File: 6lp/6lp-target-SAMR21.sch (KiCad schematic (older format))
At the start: 25 parts, among them SW1 SW_PUSH, T1 2450BM15A0015, U3 SAMR21E, X1 CRYSTAL-4

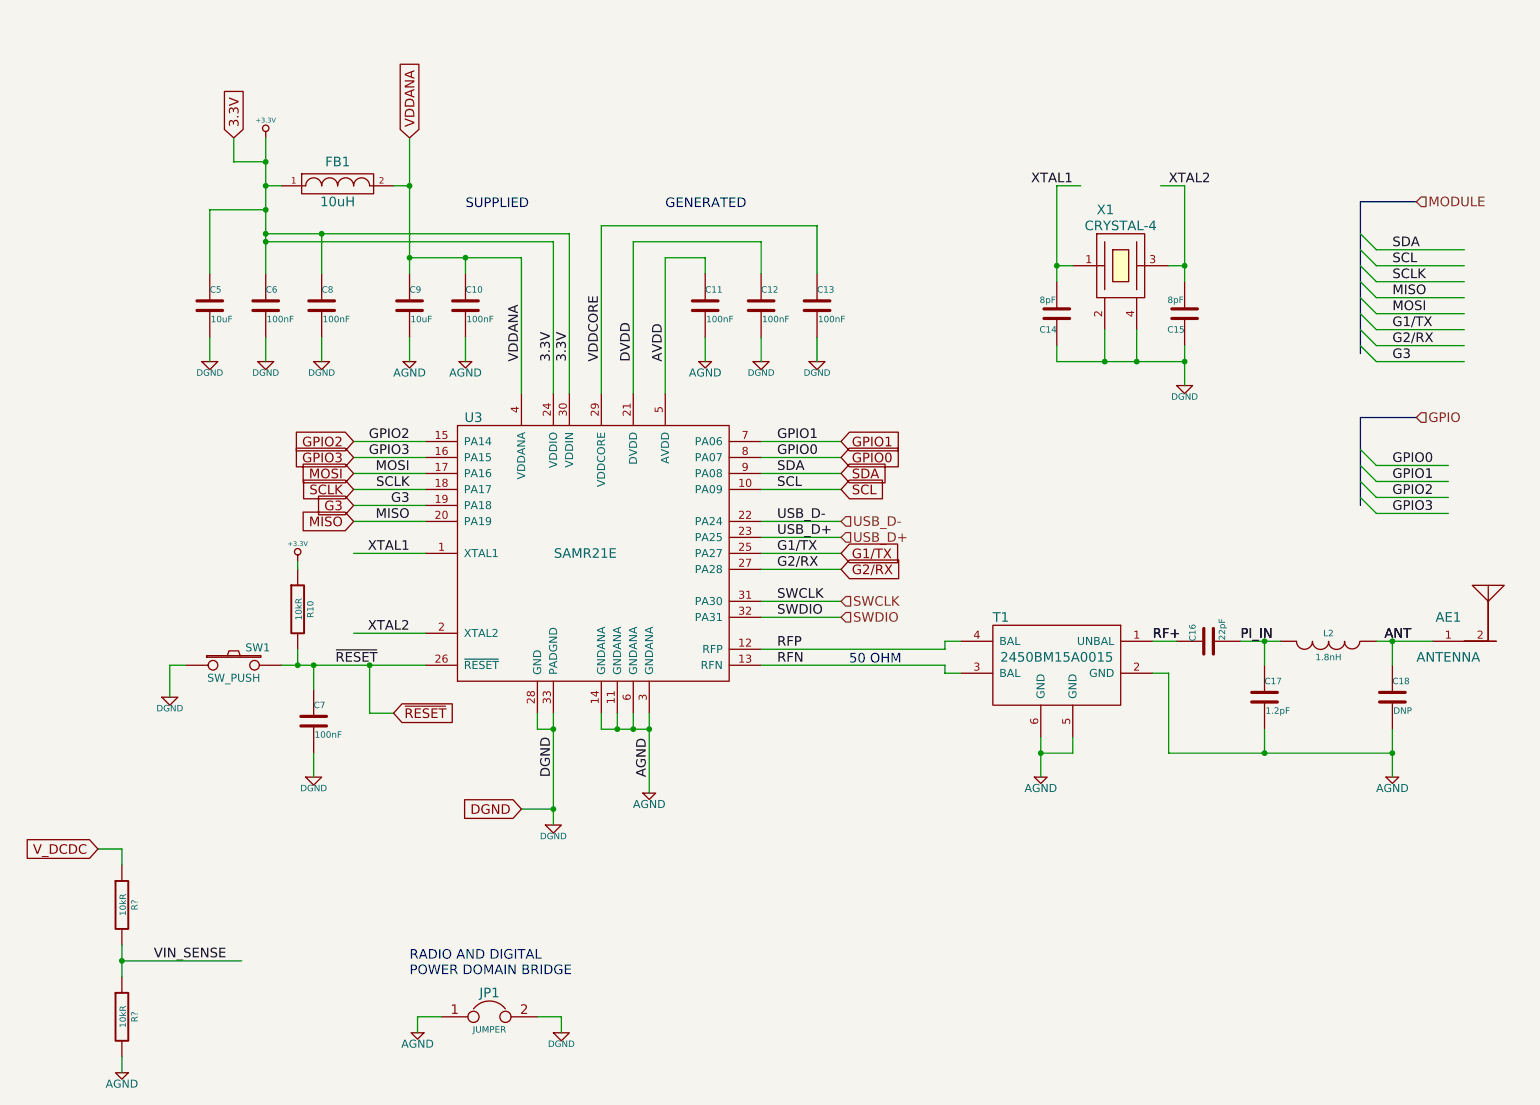
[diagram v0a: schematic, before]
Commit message: gpio rehash, netlist and component update
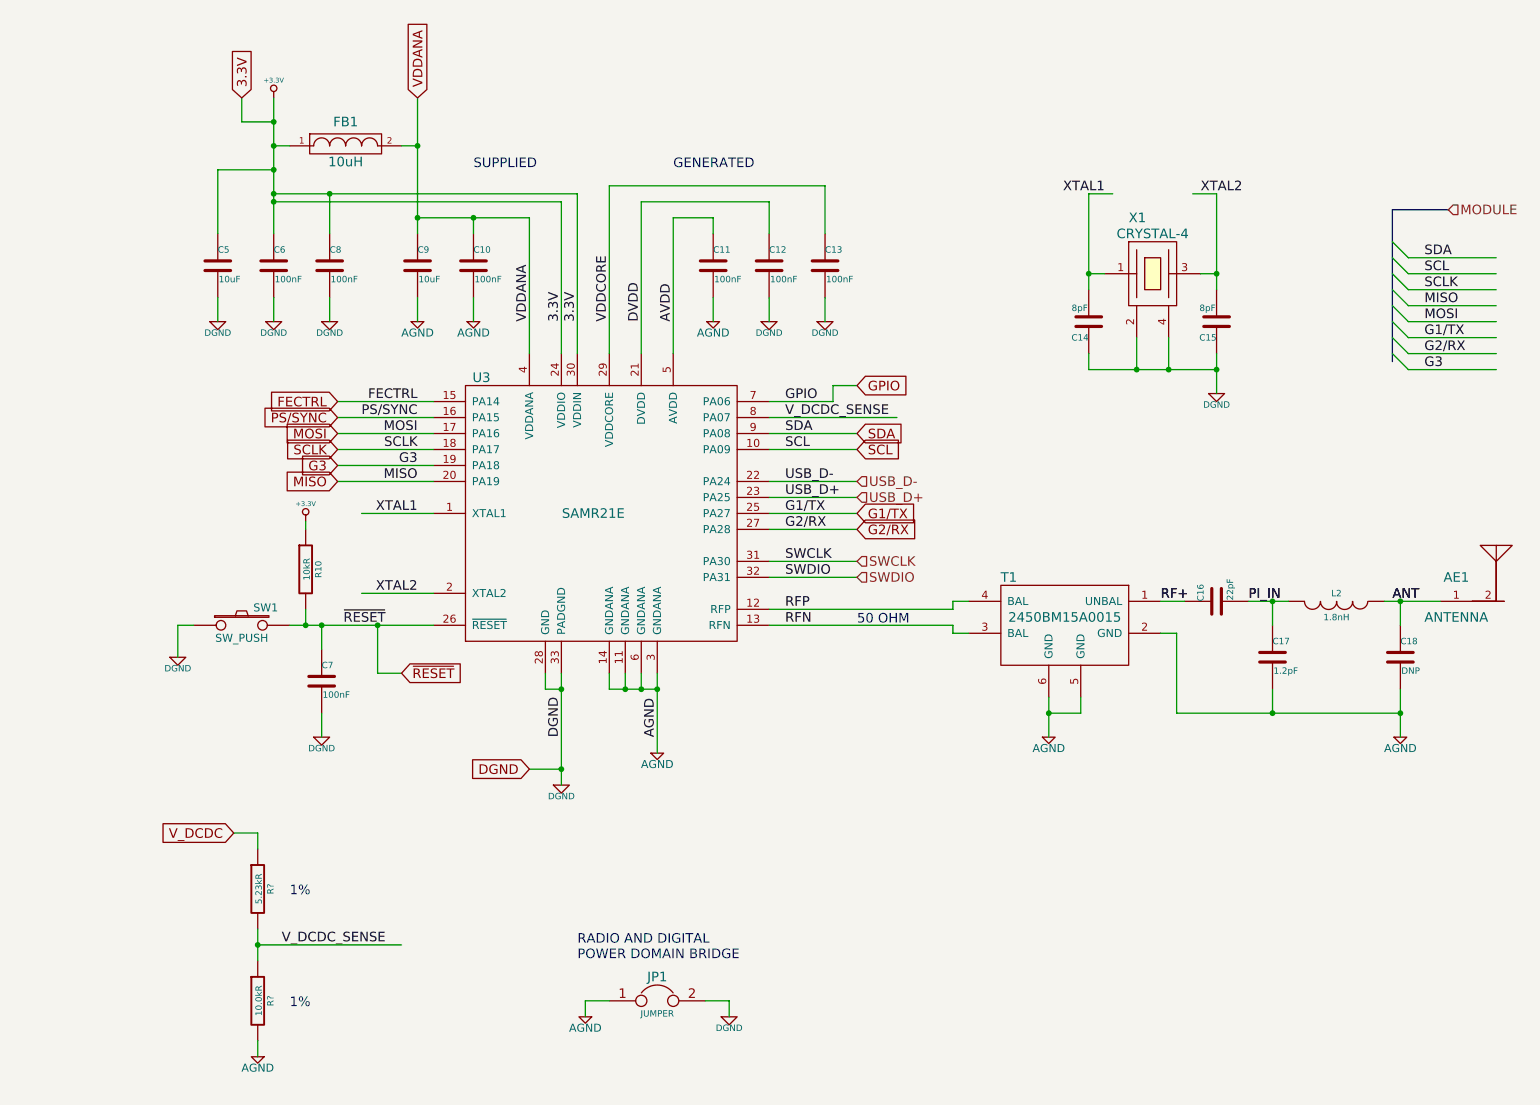
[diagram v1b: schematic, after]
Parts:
- R?: value 10kR -> 5.23kR
- R?: value 10kR -> 10.0kR
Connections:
- net labels added: FECTRL, PS/SYNC, V_DCDC_SENSE
- net labels removed: GPIO0, GPIO1, GPIO2, GPIO3, VIN_SENSE
- wire segments 120 -> 118
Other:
- note added: "1%"
- moved on the sheet: AE1, C10, C11, C12, C13, C14, C15, C16, C17, C18, C5, C6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

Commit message: don't sass me, DRC
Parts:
- gave numbers to parts that had none: 2
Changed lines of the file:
@@
 $EndDescr
 $Comp
-L AGND #PWR025
+L AGND #PWR024
 U 1 1 5453137E
 P 4700 5500
-F 0 "#PWR025" H 4700 5500 40  0001 C CNN
+F 0 "#PWR024" H 4700 5500 40  0001 C CNN
 F 1 "AGND" H 4700 5430 50  0000 C CNN
 F 2 "" H 4700 5500 60  0000 C CNN
@@
 $EndComp
 $Comp
-L DGND #PWR026
+L DGND #PWR025
 U 1 1 5453138D
 P 4100 5700
-F 0 "#PWR026" H 4100 5700 40  0001 C CNN
+F 0 "#PWR025" H 4100 5700 40  0001 C CNN
 F 1 "DGND" H 4100 5630 40  0000 C CNN
 F 2 "" H 4100 5700 60  0000 C CNN
@@
 $EndComp
 $Comp
-L DGND #PWR027
+L DGND #PWR026
 U 1 1 54531393
 P 2650 2800
-F 0 "#PWR027" H 2650 2800 40  0001 C CNN
+F 0 "#PWR026" H 2650 2800 40  0001 C CNN
 F 1 "DGND" H 2650 2730 40  0000 C CNN
 F 2 "" H 2650 2800 60  0000 C CNN
@@
 $EndComp
 $Comp
-L AGND #PWR028
+L AGND #PWR027
 U 1 1 545313BC
 P 5050 2800
-F 0 "#PWR028" H 5050 2800 40  0001 C CNN
+F 0 "#PWR027" H 5050 2800 40  0001 C CNN
 F 1 "AGND" H 5050 2730 50  0000 C CNN
 F 2 "" H 5050 2800 60  0000 C CNN
@@
 $EndComp
 $Comp
-L DGND #PWR029
+L DGND #PWR028
 U 1 1 545313C2
 P 2300 2800
-F 0 "#PWR029" H 2300 2800 40  0001 C CNN
+F 0 "#PWR028" H 2300 2800 40  0001 C CNN
 F 1 "DGND" H 2300 2730 40  0000 C CNN
 F 2 "" H 2300 2800 60  0000 C CNN
@@
 $EndComp
 $Comp
-L DGND #PWR030
+L DGND #PWR029
 U 1 1 545313C8
 P 5750 2800
-F 0 "#PWR030" H 5750 2800 40  0001 C CNN
+F 0 "#PWR029" H 5750 2800 40  0001 C CNN
 F 1 "DGND" H 5750 2730 40  0000 C CNN
 F 2 "" H 5750 2800 60  0000 C CNN
@@
 $EndComp
 $Comp
-L +3.3V #PWR031
+L +3.3V #PWR030
 U 1 1 545313CE
 P 2300 1400
-F 0 "#PWR031" H 2300 1360 30  0001 C CNN
+F 0 "#PWR030" H 2300 1360 30  0001 C CNN
 F 1 "+3.3V" H 2300 1510 30  0000 C CNN
 F 2 "" H 2300 1400 60  0000 C CNN
@@
 AVDD
 $Comp
-L DGND #PWR032
+L DGND #PWR031
 U 1 1 545313D5
 P 5400 2800
-F 0 "#PWR032" H 5400 2800 40  0001 C CNN
+F 0 "#PWR031" H 5400 2800 40  0001 C CNN
 F 1 "DGND" H 5400 2730 40  0000 C CNN
 F 2 "" H 5400 2800 60  0000 C CNN
@@
 SUPPLIED
 $Comp
-L AGND #PWR033
+L AGND #PWR032
 U 1 1 545313DF
 P 3550 2800
-F 0 "#PWR033" H 3550 2800 40  0001 C CNN
+F 0 "#PWR032" H 3550 2800 40  0001 C CNN
 F 1 "AGND" H 3550 2730 50  0000 C CNN
 F 2 "" H 3550 2800 60  0000 C CNN
@@
 $EndComp
 $Comp
-L AGND #PWR034
+L AGND #PWR033
 U 1 1 545313F5
 P 3200 2800
-F 0 "#PWR034" H 3200 2800 40  0001 C CNN
+F 0 "#PWR033" H 3200 2800 40  0001 C CNN
 F 1 "AGND" H 3200 2730 50  0000 C CNN
 F 2 "" H 3200 2800 60  0000 C CNN
@@
 $EndComp
 $Comp
-L DGND #PWR035
+L DGND #PWR034
 U 1 1 54531403
 P 1950 2800
-F 0 "#PWR035" H 1950 2800 40  0001 C CNN
+F 0 "#PWR034" H 1950 2800 40  0001 C CNN
 F 1 "DGND" H 1950 2730 40  0000 C CNN
 F 2 "" H 1950 2800 60  0000 C CNN
@@
 $EndComp
 $Comp
-L DGND #PWR036
+L DGND #PWR035
 U 1 1 54531418
 P 2600 5400
-F 0 "#PWR036" H 2600 5400 40  0001 C CNN
+F 0 "#PWR035" H 2600 5400 40  0001 C CNN
 F 1 "DGND" H 2600 5330 40  0000 C CNN
 F 2 "" H 2600 5400 60  0000 C CNN
@@
 $EndComp
 $Comp
-L +3.3V #PWR037
+L +3.3V #PWR036
 U 1 1 54531425
 P 2500 4050
-F 0 "#PWR037" H 2500 4010 30  0001 C CNN
+F 0 "#PWR036" H 2500 4010 30  0001 C CNN
 F 1 "+3.3V" H 2500 4160 30  0000 C CNN
 F 2 "" H 2500 4050 60  0000 C CNN
@@
 $EndComp
 $Comp
-L AGND #PWR038
+L AGND #PWR037
 U 1 1 54531457
 P 7150 5400
-F 0 "#PWR038" H 7150 5400 40  0001 C CNN
+F 0 "#PWR037" H 7150 5400 40  0001 C CNN
 F 1 "AGND" H 7150 5330 50  0000 C CNN
 F 2 "" H 7150 5400 60  0000 C CNN
@@
 $EndComp
 $Comp
-L AGND #PWR039
+L AGND #PWR038
 U 1 1 5453145D
 P 9350 5400
-F 0 "#PWR039" H 9350 5400 40  0001 C CNN
+F 0 "#PWR038" H 9350 5400 40  0001 C CNN
 F 1 "AGND" H 9350 5330 50  0000 C CNN
 F 2 "" H 9350 5400 60  0000 C CNN
@@
 $EndComp
 $Comp
-L DGND #PWR040
+L DGND #PWR039
 U 1 1 54531483
 P 1700 4900
-F 0 "#PWR040" H 1700 4900 40  0001 C CNN
+F 0 "#PWR039" H 1700 4900 40  0001 C CNN
 F 1 "DGND" H 1700 4830 40  0000 C CNN
 F 2 "" H 1700 4900 60  0000 C CNN
@@
 $EndComp
 $Comp
-L DGND #PWR041
+L DGND #PWR040
 U 1 1 54532400
 P 8200 3250
-F 0 "#PWR041" H 8200 3250 40  0001 C CNN
+F 0 "#PWR040" H 8200 3250 40  0001 C CNN
 F 1 "DGND" H 8200 3180 40  0000 C CNN
 F 2 "" H 8200 3250 60  0000 C CNN
@@
 RADIO AND DIGITAL\nPOWER DOMAIN BRIDGE
 $Comp
-L AGND #PWR042
+L AGND #PWR041
 U 1 1 54539592
 P 4250 7150
-F 0 "#PWR042" H 4250 7150 40  0001 C CNN
+F 0 "#PWR041" H 4250 7150 40  0001 C CNN
 F 1 "AGND" H 4250 7080 50  0000 C CNN
 F 2 "" H 4250 7150 60  0000 C CNN
@@
 $EndComp
 $Comp
-L DGND #PWR043
+L DGND #PWR042
 U 1 1 54539598
 P 5150 7150
-F 0 "#PWR043" H 5150 7150 40  0001 C CNN
+F 0 "#PWR042" H 5150 7150 40  0001 C CNN
 F 1 "DGND" H 5150 7080 40  0000 C CNN
 F 2 "" H 5150 7150 60  0000 C CNN
@@
 V_DCDC
 $Comp
-L R R?
+L R R9
 U 1 1 54540406
 P 2200 6350
-F 0 "R?" V 2280 6350 40  0000 C CNN
+F 0 "R9" V 2280 6350 40  0000 C CNN
 F 1 "5.23kR" V 2207 6351 40  0000 C CNN
 F 2 "parts:SMD-0402" V 2130 6350 30  0001 C CNN
@@
 $EndComp
 $Comp
-L R R?
+L R R11
 U 1 1 54541C36
 P 2200 7050
-F 0 "R?" V 2280 7050 40  0000 C CNN
+F 0 "R11" V 2280 7050 40  0000 C CNN
 F 1 "10.0kR" V 2207 7051 40  0000 C CNN
 F 2 "parts:SMD-0402" V 2130 7050 30  0001 C CNN
@@
 $EndComp
 $Comp
-L AGND #PWR?
+L AGND #PWR043
 U 1 1 54541CB9
 P 2200 7400
-F 0 "#PWR?" H 2200 7400 40  0001 C CNN
+F 0 "#PWR043" H 2200 7400 40  0001 C CNN
 F 1 "AGND" H 2200 7330 50  0000 C CNN
 F 2 "" H 2200 7400 60  0000 C CNN

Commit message: let's make a board!
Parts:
- X1: value CRYSTAL-4 -> 16.0000MF09Z-AC3
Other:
- moved on the sheet: C14, C15
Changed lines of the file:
@@
 L C C15
 U 1 1 545323F2
-P 8200 2800
-F 0 "C15" H 8200 2900 40  0000 L CNN
-F 1 "8pF" H 8206 2715 40  0000 L CNN
-F 2 "parts:SMD-0402" H 8238 2650 30  0001 C CNN
-F 3 "" H 8200 2800 60  0000 C CNN
-	1    8200 2800
+P 8350 2800
+F 0 "C15" H 8350 2900 40  0000 L CNN
+F 1 "8pF" H 8356 2715 40  0000 L CNN
+F 2 "parts:SMD-0402" H 8388 2650 30  0001 C CNN
+F 3 "" H 8350 2800 60  0000 C CNN
+	1    8350 2800
 	-1   0    0    1
 $EndComp
@@
 L C C14
 U 1 1 545323F9
-P 7400 2800
-F 0 "C14" H 7400 2900 40  0000 L CNN
-F 1 "8pF" H 7406 2715 40  0000 L CNN
-F 2 "parts:SMD-0402" H 7438 2650 30  0001 C CNN
-F 3 "" H 7400 2800 60  0000 C CNN
-	1    7400 2800
+P 7250 2800
+F 0 "C14" H 7250 2900 40  0000 L CNN
+F 1 "8pF" H 7256 2715 40  0000 L CNN
+F 2 "parts:SMD-0402" H 7288 2650 30  0001 C CNN
+F 3 "" H 7250 2800 60  0000 C CNN
+	1    7250 2800
 	-1   0    0    1
 $EndComp
@@
 L DGND #PWR040
 U 1 1 54532400
-P 8200 3250
-F 0 "#PWR040" H 8200 3250 40  0001 C CNN
-F 1 "DGND" H 8200 3180 40  0000 C CNN
-F 2 "" H 8200 3250 60  0000 C CNN
-F 3 "" H 8200 3250 60  0000 C CNN
-	1    8200 3250
+P 8350 3250
+F 0 "#PWR040" H 8350 3250 40  0001 C CNN
+F 1 "DGND" H 8350 3180 40  0000 C CNN
+F 2 "" H 8350 3250 60  0000 C CNN
+F 3 "" H 8350 3250 60  0000 C CNN
+	1    8350 3250
 	1    0    0    -1
 $EndComp
-Text Label 7500 2000 2    60   ~ 0
+Text Label 7350 2000 2    60   ~ 0
 XTAL1
-Text Label 8100 2000 0    60   ~ 0
+Text Label 8250 2000 0    60   ~ 0
 XTAL2
 $Comp
@@
 P 7800 2500
 F 0 "X1" H 7650 2850 60  0000 L CNN
-F 1 "CRYSTAL-4" H 7800 2750 60  0000 C CNN
+F 1 "16.0000MF09Z-AC3" H 7800 2750 60  0000 C CNN
 F 2 "parts:TSX-3225" H 7800 2500 60  0001 C CNN
 F 3 "" H 7800 2500 60  0000 C CNN
@@
 	1    0    0    -1
 $EndComp
-Connection ~ 8200 2500
+Connection ~ 8350 2500
 Wire Wire Line
-	8100 2500 8200 2500
-Connection ~ 7400 2500
+	8100 2500 8350 2500
+Connection ~ 7250 2500
 Wire Wire Line
-	7400 2500 7500 2500
+	7250 2500 7500 2500
 Wire Wire Line
-	8200 3000 8200 3250
+	8350 3000 8350 3250
 Wire Wire Line
-	7400 3100 8200 3100
+	7250 3100 8350 3100
 Wire Wire Line
 	7700 2900 7700 3100
@@
 Connection ~ 7900 3100
 Wire Wire Line
-	8050 2000 8200 2000
+	7950 2000 8350 2000
 Wire Wire Line
-	8200 2000 8200 2600
+	8350 2000 8350 2600
 Wire Wire Line
-	7400 2000 7400 2600
+	7250 2000 7250 2600
 Wire Wire Line
-	7400 2000 7550 2000
-Connection ~ 8200 3100
+	7250 2000 7450 2000
+Connection ~ 8350 3100
 Wire Wire Line
-	7400 3000 7400 3100
+	7250 3000 7250 3100
 Text Notes 4200 6800 0    60   ~ 0
 RADIO AND DIGITAL\nPOWER DOMAIN BRIDGE
